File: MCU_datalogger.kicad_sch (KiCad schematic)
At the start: 0 parts

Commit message: Modified Schematic
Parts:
- added BT1: Battery, symbol Device:Battery
- added C1, C2, C3, C4: C, symbol Device:C
- added C5: C_Polarized, symbol Device:C_Polarized
- added D1, D2: LED, symbol Device:LED
- added H1, H2, H3, H4: MountingHole, symbol Mechanical:MountingHole
- added R1, R2, R3, R4, R5: R, symbol Device:R
- added U1, U2: 24LC1025, symbol Memory_EEPROM:24LC1025
- added U3: DS1337S_, DS1337S_:SOIC127P600X175-8N, symbol DS1337S_:DS1337S_
- added U4: ATMEGA328P-AU, ATMEGA328P-AU:QFP80P900X900X120-32N, symbol ATMEGA328P-AU:ATMEGA328P-AU
- added Y1, Y2: Crystal, symbol Device:Crystal
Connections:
- new net GND: U4.21 (GND), U4.3 (GND), U4.5 (GND)
- new net VCC: U4.4 (VCC), U4.6 (VCC)
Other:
- added sheet connectors (connectors.kicad_sch)
- title: (none) -> ${project_name}

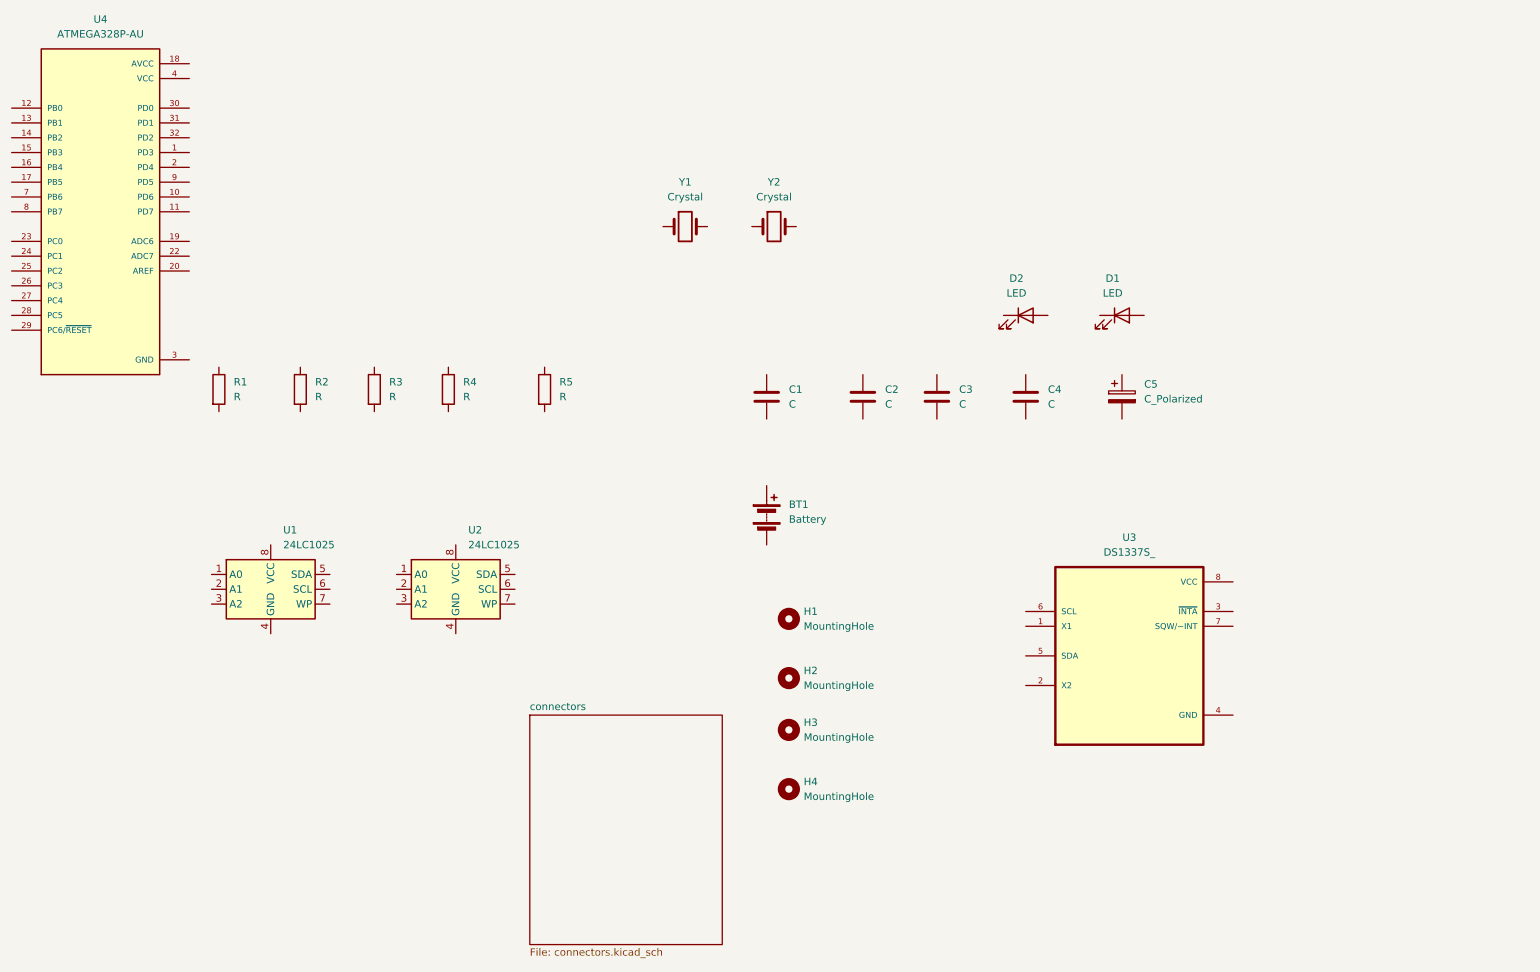
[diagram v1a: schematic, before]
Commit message: Arranged and annotated the schematic
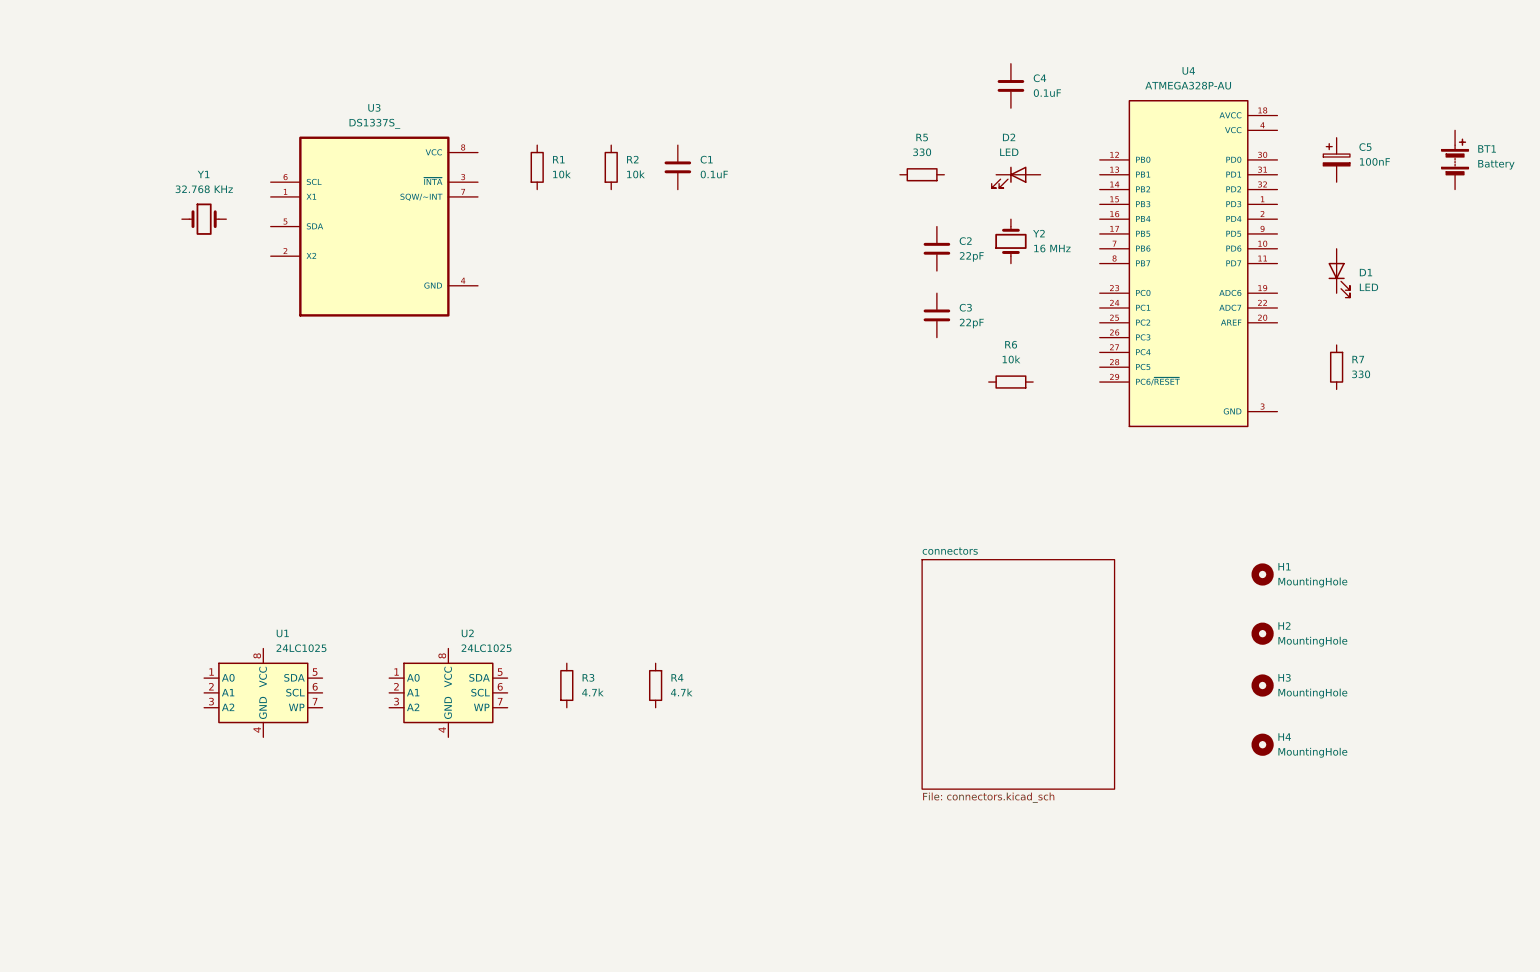
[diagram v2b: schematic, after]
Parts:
- added R6: 10k, symbol Device:R
- added R7: 330, symbol Device:R
- C1, C4: value C -> 0.1uF
- C2, C3: value C -> 22pF
- C5: value C_Polarized -> 100nF
- R1, R2: value R -> 10k
- R3, R4: value R -> 4.7k
- R5: value R -> 330
- Y1: value Crystal -> 32.768 KHz
- Y2: value Crystal -> 16 MHz
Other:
- moved on the sheet: BT1, C1, C2, C3, C4, C5, D1, D2, H1, H2, H3, H4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

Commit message: Assigned footprints to symbols
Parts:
- BT1: footprint (none) -> Connector_PinHeader_2.54mm:PinHeader_1x02_P2.54mm_Vertical
- C1, C2, C3, C4, C5: footprint (none) -> Capacitor_SMD:C_0805_2012Metric
- D1, D2: footprint (none) -> LED_SMD:LED_0805_2012Metric
- H1, H2, H3, H4: footprint (none) -> MountingHole:MountingHole_2.1mm
- R1, R2, R3, R4, R5, R6, R7: footprint (none) -> Resistor_SMD:R_0805_2012Metric
- U1, U2: footprint (none) -> Package_SO:SOIC-8_5.3x5.3mm_P1.27mm
- Y1, Y2: footprint (none) -> Crystal:Crystal_SMD_5032-2Pin_5.0x3.2mm_HandSoldering
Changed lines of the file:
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@@
 			)
 		)
-		(property "Footprint" ""
+		(property "Footprint" "MountingHole:MountingHole_2.1mm"
 			(at 237.49 148.59 0)
 			(effects
@@
 			)
 		)
-		(property "Footprint" ""
+		(property "Footprint" "Crystal:Crystal_SMD_5032-2Pin_5.0x3.2mm_HandSoldering"
 			(at 55.88 58.42 0)
 			(effects
@@
 			)
 		)
-		(property "Footprint" ""
+		(property "Footprint" "Capacitor_SMD:C_0805_2012Metric"
 			(at 182.5752 78.74 0)
 			(effects
@@
 			)
 		)
-		(property "Footprint" ""
+		(property "Footprint" "Capacitor_SMD:C_0805_2012Metric"
 			(at 251.1552 52.07 0)
 			(effects
@@
 			)
 		)
-		(property "Footprint" ""
+		(property "Footprint" "Resistor_SMD:R_0805_2012Metric"
 			(at 123.952 49.53 90)
 			(effects
@@
 			)
 		)
-		(property "Footprint" ""
+		(property "Footprint" "Crystal:Crystal_SMD_5032-2Pin_5.0x3.2mm_HandSoldering"
 			(at 194.31 62.23 0)
 			(effects
@@
 			)
 		)
-		(property "Footprint" ""
+		(property "Footprint" "MountingHole:MountingHole_2.1mm"
 			(at 237.49 129.54 0)
 			(effects
@@
 			)
 		)
-		(property "Footprint" ""
+		(property "Footprint" "Capacitor_SMD:C_0805_2012Metric"
 			(at 195.2752 39.37 0)
 			(effects
@@
 			)
 		)
-		(property "Footprint" ""
+		(property "Footprint" "Resistor_SMD:R_0805_2012Metric"
 			(at 135.128 138.43 90)
 			(effects
@@
 			)
 		)
-		(property "Footprint" ""
+		(property "Footprint" "Connector_PinHeader_2.54mm:PinHeader_1x02_P2.54mm_Vertical"
 			(at 270.51 46.736 90)
 			(effects
@@
 			)
 		)
-		(property "Footprint" ""
+		(property "Footprint" "MountingHole:MountingHole_2.1mm"
 			(at 237.49 138.43 0)
 			(effects
@@
 			)
 		)
-		(property "Footprint" ""
+		(property "Footprint" "Resistor_SMD:R_0805_2012Metric"
 			(at 116.332 138.43 90)
 			(effects
@@
 			)
 		)
-		(property "Footprint" ""
+		(property "Footprint" "Capacitor_SMD:C_0805_2012Metric"
 			(at 138.1252 53.34 0)
 			(effects
@@
 			)
 		)
-		(property "Footprint" ""
+		(property "Footprint" "MountingHole:MountingHole_2.1mm"
 			(at 237.49 119.38 0)
 			(effects
@@
 			)
 		)
-		(property "Footprint" ""
+		(property "Footprint" "Package_SO:SOIC-8_5.3x5.3mm_P1.27mm"
 			(at 66.04 139.7 0)
 			(effects
@@
 			)
 		)
-		(property "Footprint" ""
+		(property "Footprint" "Resistor_SMD:R_0805_2012Metric"
 			(at 194.31 88.138 90)
 			(effects
@@
 			)
 		)
-		(property "Footprint" ""
+		(property "Footprint" "Resistor_SMD:R_0805_2012Metric"
 			(at 251.968 83.82 90)
 			(effects
@@
 			)
 		)
-		(property "Footprint" ""
+		(property "Footprint" "LED_SMD:LED_0805_2012Metric"
 			(at 195.58 50.8 0)
 			(effects
@@
 			)
 		)
-		(property "Footprint" ""
+		(property "Footprint" "Resistor_SMD:R_0805_2012Metric"
 			(at 111.252 49.53 90)
 			(effects
@@
 			)
 		)
-		(property "Footprint" ""
+		(property "Footprint" "Capacitor_SMD:C_0805_2012Metric"
 			(at 182.5752 67.31 0)
 			(effects
@@
 			)
 		)
-		(property "Footprint" ""
+		(property "Footprint" "Package_SO:SOIC-8_5.3x5.3mm_P1.27mm"
 			(at 97.79 139.7 0)
 			(effects
@@
 			)
 		)
-		(property "Footprint" ""
+		(property "Footprint" "LED_SMD:LED_0805_2012Metric"
 			(at 250.19 67.31 0)
 			(effects
@@
 			)
 		)
-		(property "Footprint" ""
+		(property "Footprint" "Resistor_SMD:R_0805_2012Metric"
 			(at 179.07 52.578 90)
 			(effects

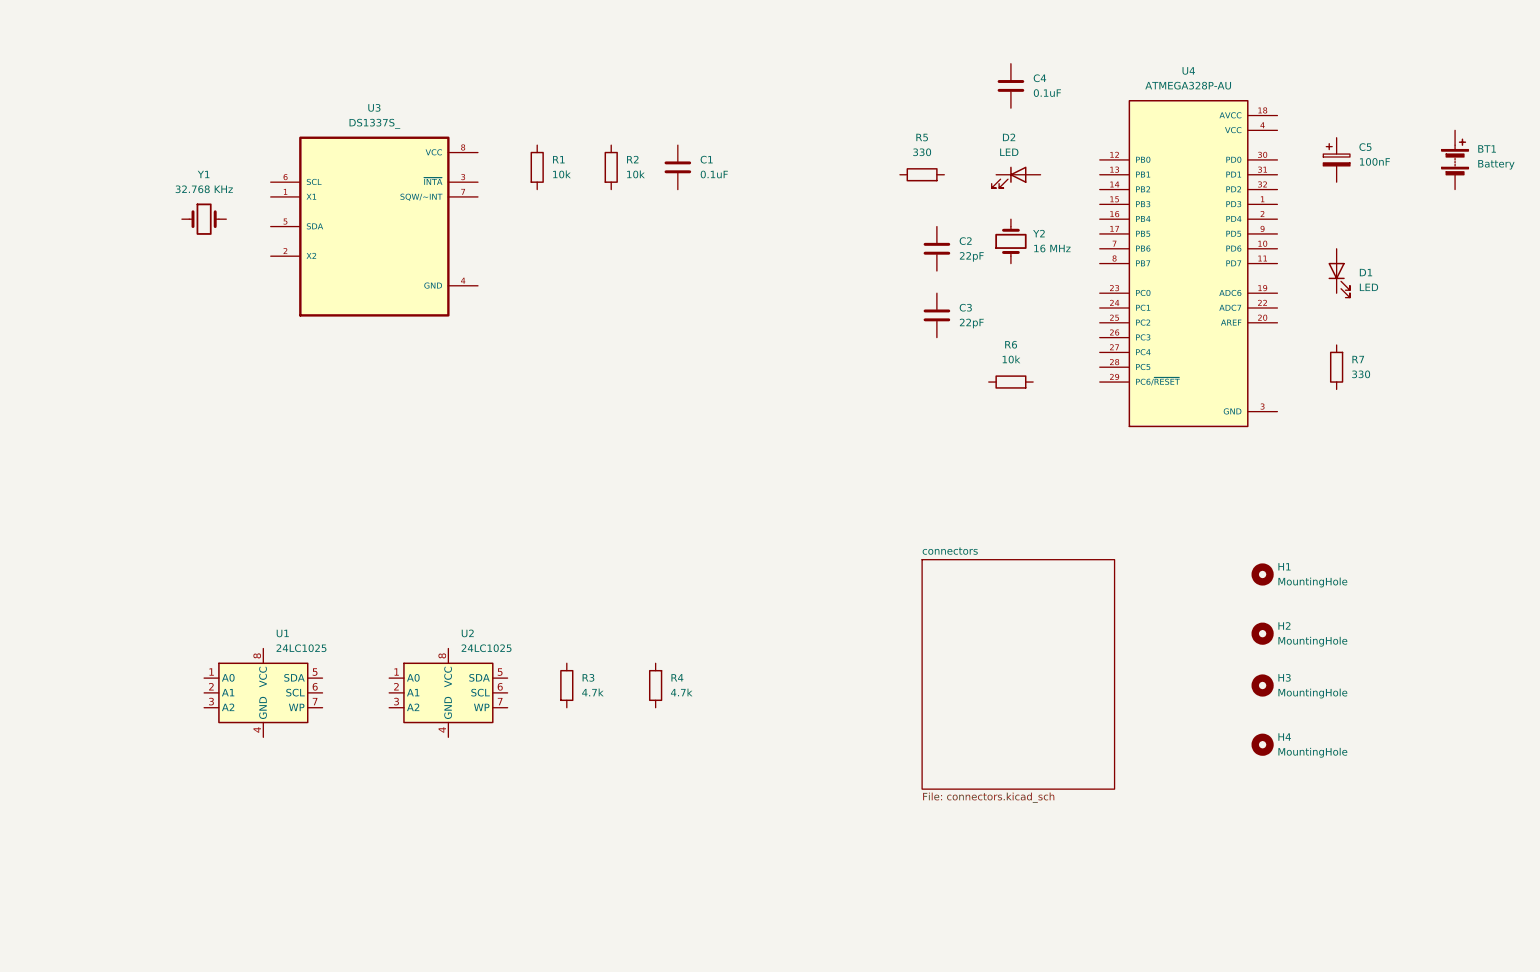
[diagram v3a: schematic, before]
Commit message: Completed wiring of main sheet
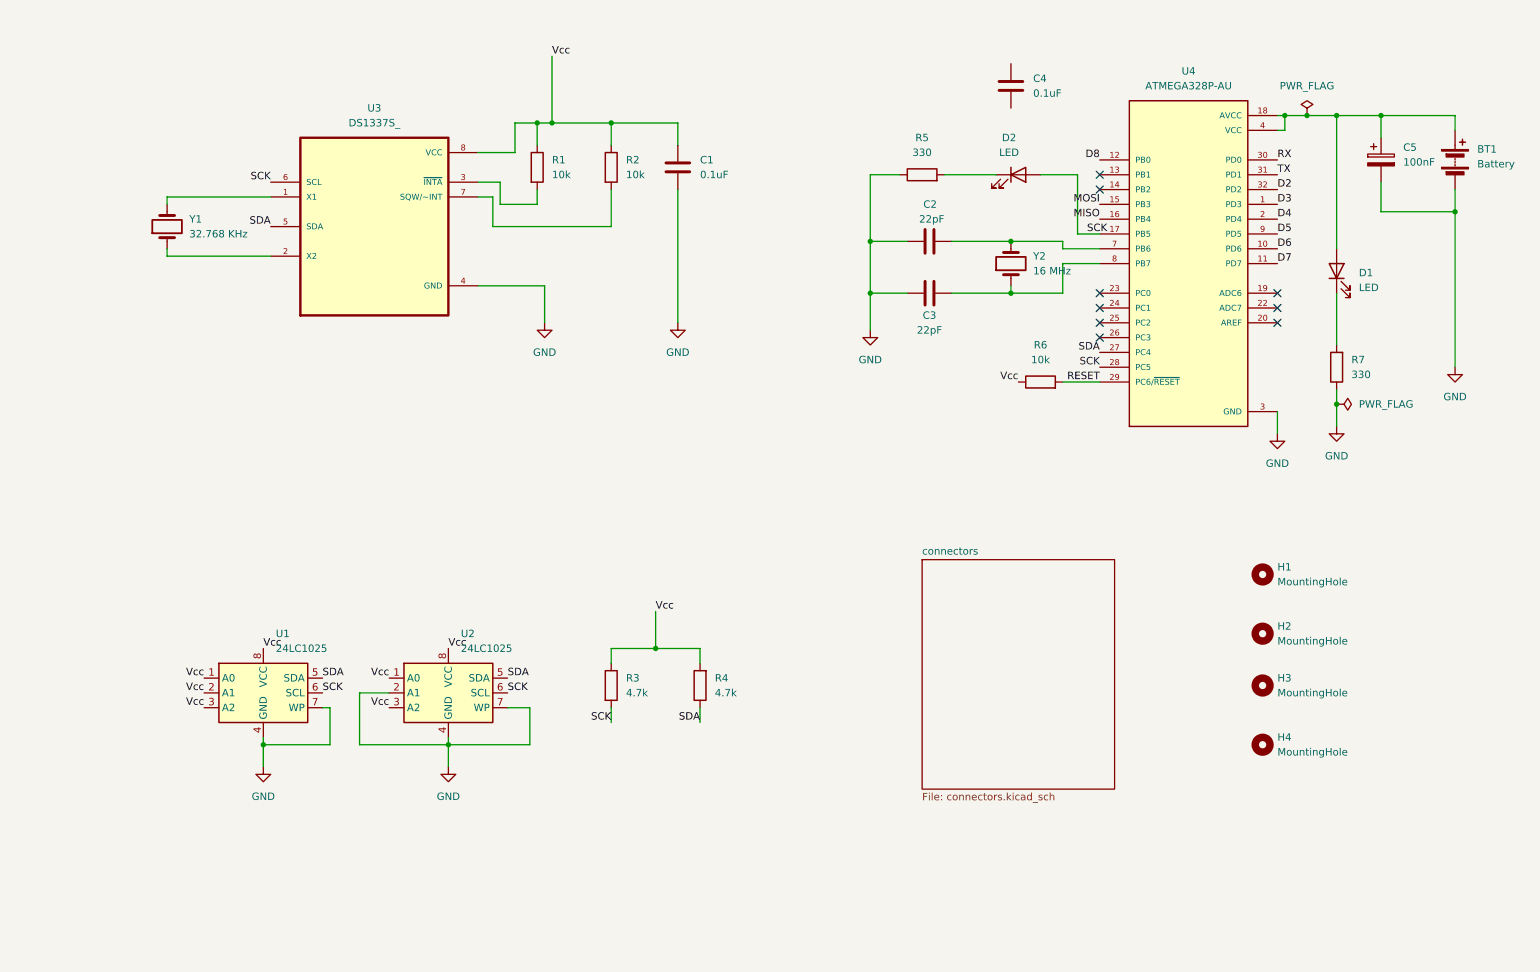
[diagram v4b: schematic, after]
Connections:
- net GND: now also BT1.2 (-), C1.2, C2.1, C3.1, C5.2, R5.1, R7.1, U1.4 (GND), U1.7 (WP), U2.2 (A1), U2.4 (GND), U2.7 (WP), U3.4 (GND)
- net VCC: now also BT1.1 (+), C5.1, D1.2 (A), U4.18 (AVCC)
- net at Y1.1: now also U3.2 (X2)
- net at Y1.2: now also U3.1 (X1)
- net at C3.2: now also U4.8 (PB7), Y2.1
- net D3: now reaches U4.1 (PD3)
- net D6: now reaches U4.10 (PD6)
- net D7: now reaches U4.11 (PD7)
- net D8: now reaches U4.12 (PB0)
- net MOSI: now reaches U4.15 (PB3)
- net MISO: now reaches U4.16 (PB4)
- net at U4.17 (PB5): now also D2.2 (A)
- net D4: now reaches U4.2 (PD4)
- net SDA: now reaches U4.27 (PC4)
- net SDA: now also R4.1, U1.5 (SDA), U2.5 (SDA), U3.5 (SDA)
- net SCK: now reaches U4.28 (PC5)
- net SCK: now also R3.2, U1.6 (SCL), U2.6 (SCL), U3.6 (SCL)
- net RESET: now reaches U4.29 (PC6/~{RESET})
- net RESET: now also R6.2
- net RX: now reaches U4.30 (PD0)
- net TX: now reaches U4.31 (PD1)
- net D2: now reaches U4.32 (PD2)
- net at U4.7 (PB6): now also C2.2, Y2.2
- net D5: now reaches U4.9 (PD5)
- net at U3.3 (~{INTA}): now also R1.2
- net at U3.7 (SQW/~INT): now also R2.2
- net Vcc: now reaches U3.8 (VCC)
- net Vcc: now also C1.1, R1.1, R2.1, R3.1, R4.2, R6.1, U1.1 (A0), U1.2 (A1), U1.3 (A2), U1.8 (VCC), U2.1 (A0), U2.3 (A2), U2.8 (VCC)
- net at R7.2: now also D1.1 (K)
- net at D2.1 (K): now also R5.2
- no-connect marks 0 -> 9
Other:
- moved on the sheet: C2, C3, C5, R3, R4, R6, Y1, Y2

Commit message: Completed wiring in secondary sheet
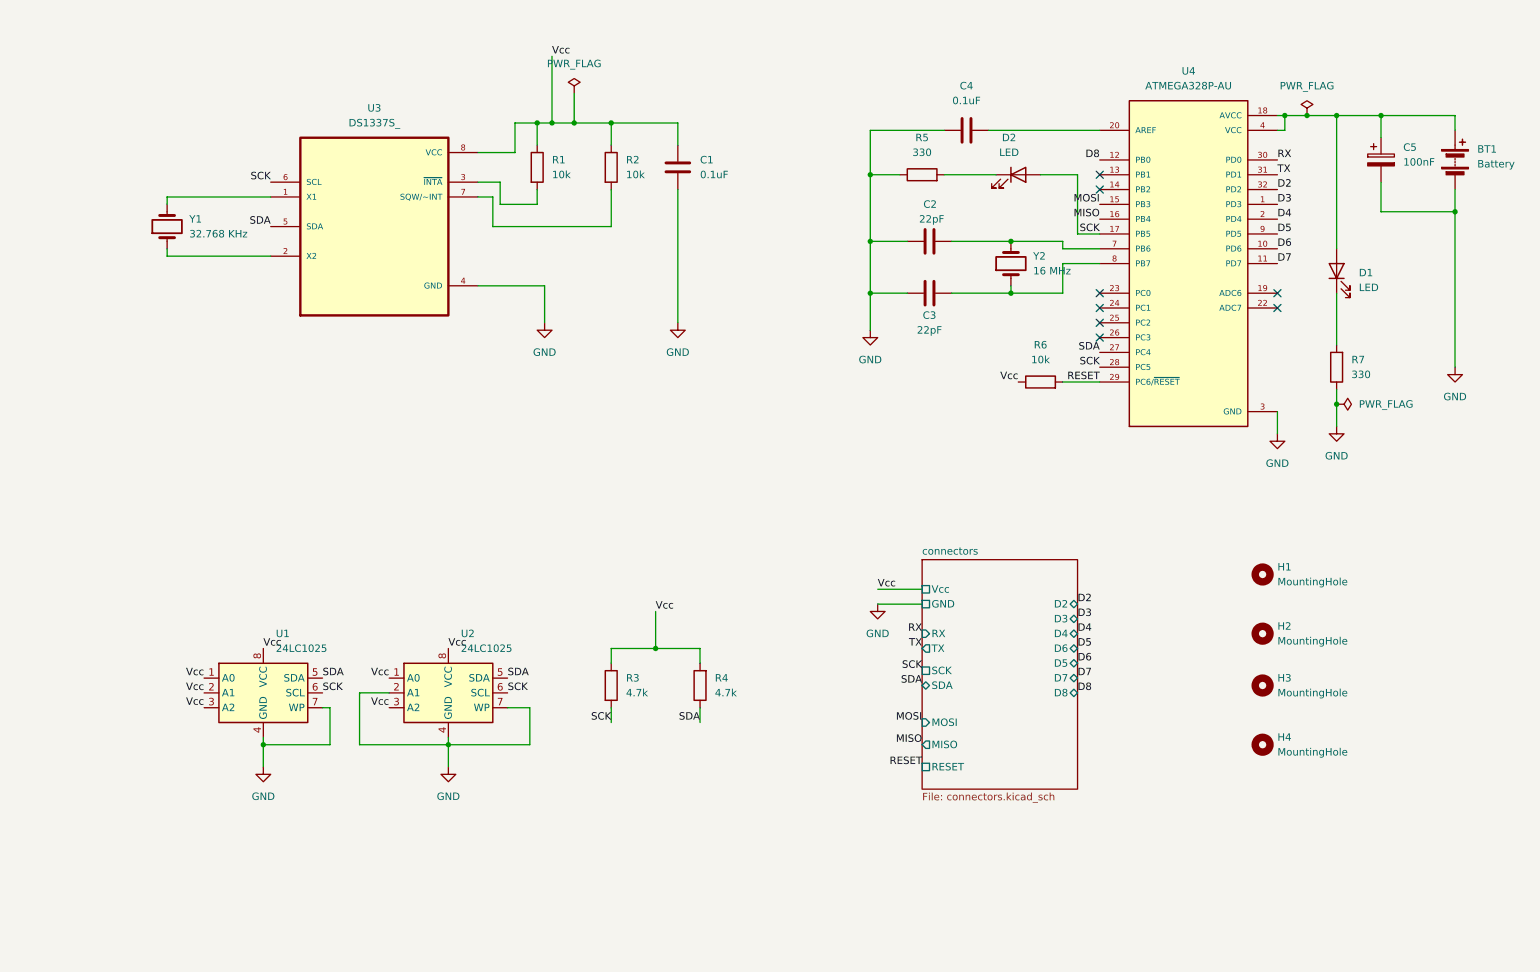
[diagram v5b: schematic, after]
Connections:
- net GND: now also C4.1
- net SCK: now also D2.2 (A), U4.17 (PB5)
- net at U4.20 (AREF): now also C4.2
- no-connect marks 9 -> 8
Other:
- sheet connectors ports: added D2, D3, D4, D5, D6, D7, D8, GND, MISO, MOSI, RESET, RX, SCK, SDA, TX, Vcc; removed none
- moved on the sheet: C4
